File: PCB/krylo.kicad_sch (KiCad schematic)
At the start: 50 parts, among them SW1 Switch, SW10 Switch, SW11 Switch, SW12 Switch, SW13 Switch, SW14 Switch, SW15 Switch, SW16 Switch, SW2 Switch, SW3 Switch, SW4 Switch, SW5 Switch, SW6 Switch, SW7 Switch, SW8 Switch, SW9 Switch, U1 nice_nano

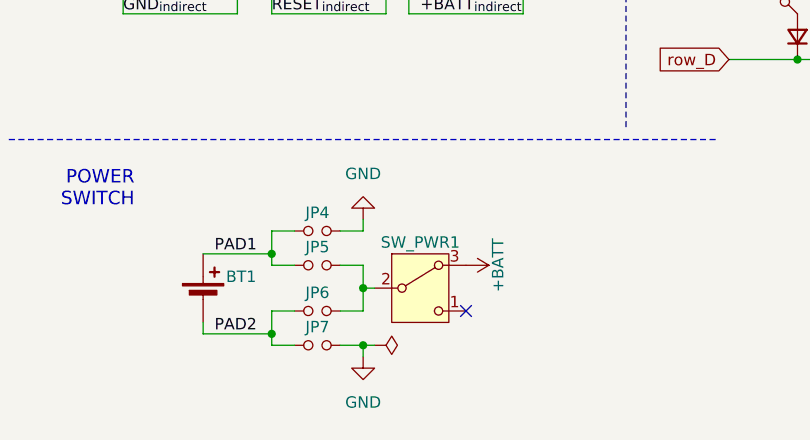
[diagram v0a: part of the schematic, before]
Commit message: Schematic is made so that it contains the double sided PCB configuration. The power component is now (conceptually) contains two switches and routes them accordingly.
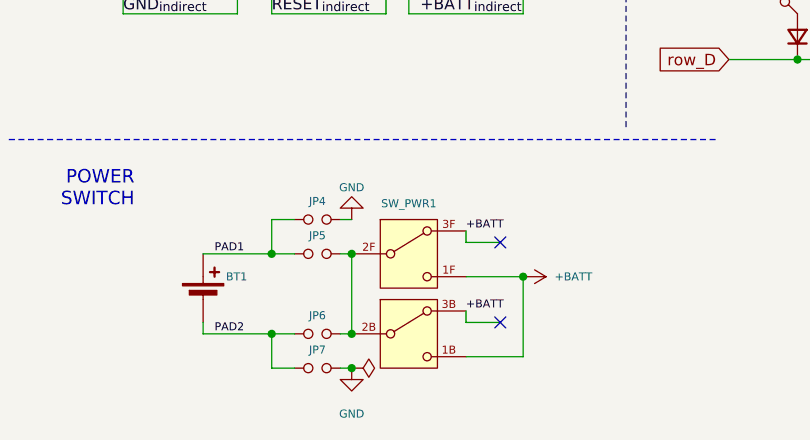
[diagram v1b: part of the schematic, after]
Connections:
- net +BATT: now also SW_PWR1.1B (C_back), SW_PWR1.1F (C_front), SW_PWR1.3B (A_back), SW_PWR1.3F (A_front); no longer SW_PWR1.3 (A)
- net at JP5.2, JP6.2: now also SW_PWR1.2B (B_back), SW_PWR1.2F (B_front); no longer SW_PWR1.2 (B)
- no-connect marks 10 -> 11
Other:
- moved on the sheet: JP4, JP5, JP6, JP7

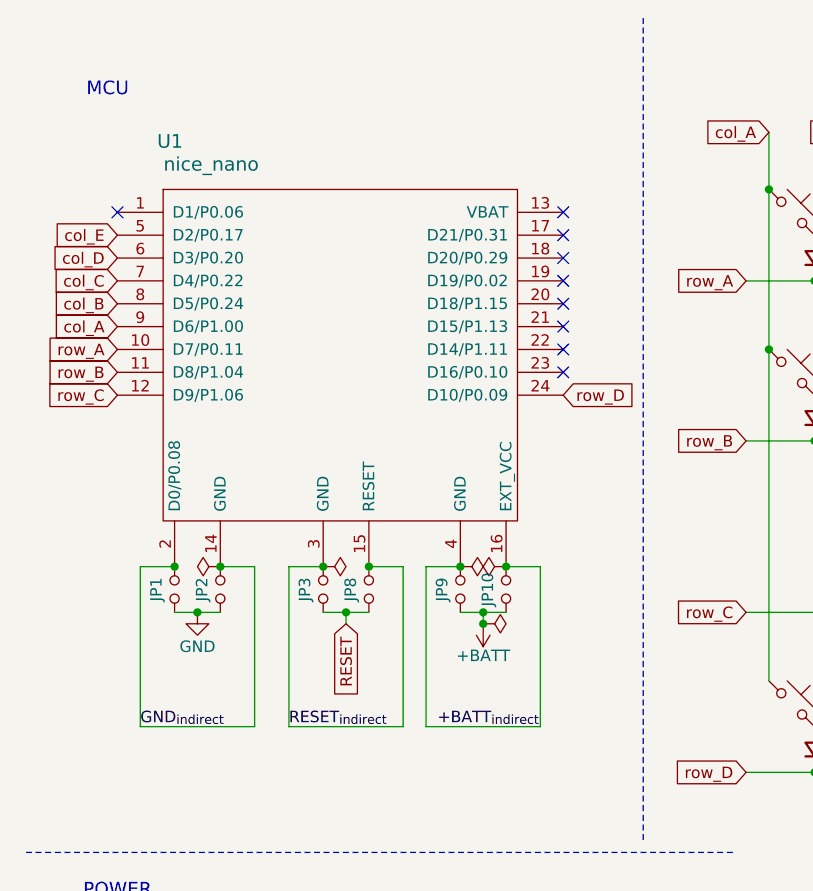
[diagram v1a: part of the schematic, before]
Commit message: Fix: correction of the MCU top/bottom pin usage and placement as well as silkscreen corrections
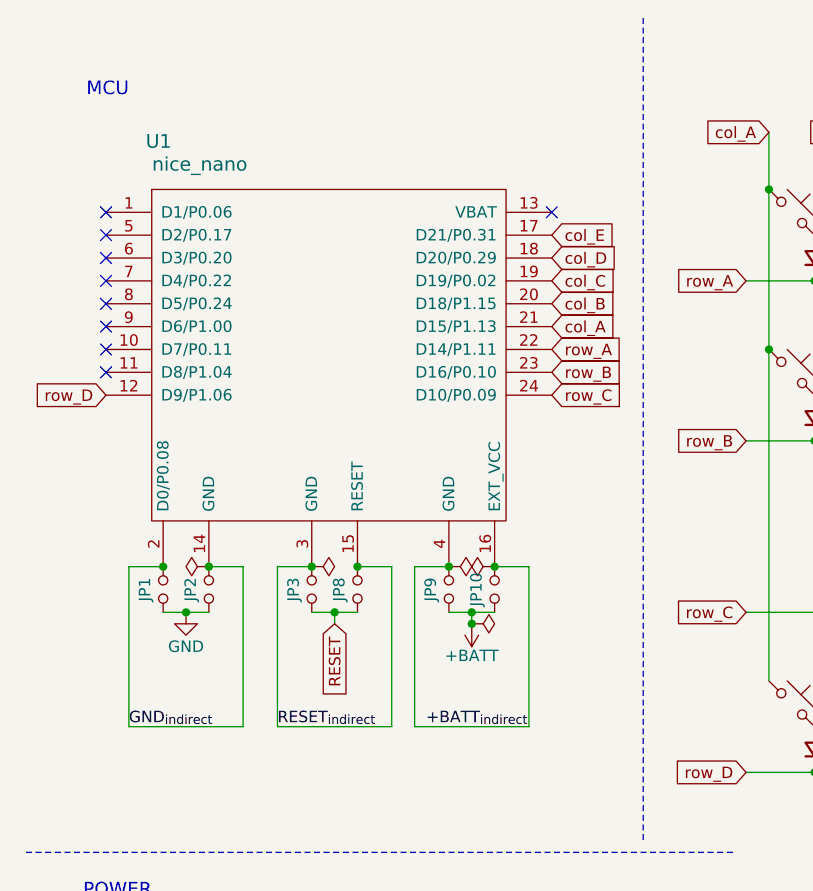
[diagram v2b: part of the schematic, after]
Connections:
- net col_A: now also U1.21 (D15/P1.13); no longer U1.9 (D6/P1.00)
- net col_B: now also U1.20 (D18/P1.15); no longer U1.8 (D5/P0.24)
- net col_C: now also U1.19 (D19/P0.02); no longer U1.7 (D4/P0.22)
- net col_D: now also U1.18 (D20/P0.29); no longer U1.6 (D3/P0.20)
- net col_E: now also U1.17 (D21/P0.31); no longer U1.5 (D2/P0.17)
- net row_A: now also U1.22 (D14/P1.11); no longer U1.10 (D7/P0.11)
- net row_B: now also U1.23 (D16/P0.10); no longer U1.11 (D8/P1.04)
- net row_C: now also U1.24 (D10/P0.09); no longer U1.12 (D9/P1.06)
- net row_D: now also U1.12 (D9/P1.06); no longer U1.24 (D10/P0.09)
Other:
- moved on the sheet: JP1, JP10, JP2, JP3, JP8, JP9, U1

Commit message: Jumper reference numbers are sorted
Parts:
- renumbered JP4 to JP1, JP5 to JP2, JP6 to JP3, JP7 to JP4, JP1 to JP5, JP2 to JP6, JP3 to JP7
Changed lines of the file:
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@@
 		(in_pos_files yes)
 		(dnp no)
-		(property "Reference" "JP1"
+		(property "Reference" "JP5"
 			(at 24.638 74.93 0)
 			(show_name no)
@@
 			(project "krylo"
 				(path "/231ead31-262f-44fe-a25c-f58d2465dcca"
-					(reference "JP1")
+					(reference "JP5")
 					(unit 1)
 				)
@@
 		(in_pos_files yes)
 		(dnp no)
-		(property "Reference" "JP6"
+		(property "Reference" "JP3"
 			(at 45.72 123.698 0)
 			(show_name no)
@@
 			(project "krylo"
 				(path "/231ead31-262f-44fe-a25c-f58d2465dcca"
-					(reference "JP6")
+					(reference "JP3")
 					(unit 1)
 				)
@@
 		(in_pos_files yes)
 		(dnp no)
-		(property "Reference" "JP4"
+		(property "Reference" "JP1"
 			(at 45.72 110.998 0)
 			(show_name no)
@@
 			(project "krylo"
 				(path "/231ead31-262f-44fe-a25c-f58d2465dcca"
-					(reference "JP4")
+					(reference "JP1")
 					(unit 1)
 				)
@@
 		(in_pos_files yes)
 		(dnp no)
-		(property "Reference" "JP2"
+		(property "Reference" "JP6"
 			(at 29.718 74.93 0)
 			(show_name no)
@@
 			(project "krylo"
 				(path "/231ead31-262f-44fe-a25c-f58d2465dcca"
-					(reference "JP2")
+					(reference "JP6")
 					(unit 1)
 				)
@@
 		(in_pos_files yes)
 		(dnp no)
-		(property "Reference" "JP7"
+		(property "Reference" "JP4"
 			(at 45.72 127.508 0)
 			(show_name no)
@@
 			(project "krylo"
 				(path "/231ead31-262f-44fe-a25c-f58d2465dcca"
-					(reference "JP7")
+					(reference "JP4")
 					(unit 1)
 				)
@@
 		(in_pos_files yes)
 		(dnp no)
-		(property "Reference" "JP5"
+		(property "Reference" "JP2"
 			(at 45.72 114.808 0)
 			(show_name no)
@@
 			(project "krylo"
 				(path "/231ead31-262f-44fe-a25c-f58d2465dcca"
-					(reference "JP5")
+					(reference "JP2")
 					(unit 1)
 				)
@@
 		(in_pos_files yes)
 		(dnp no)
-		(property "Reference" "JP3"
+		(property "Reference" "JP7"
 			(at 41.148 74.93 0)
 			(show_name no)
@@
 			(project "krylo"
 				(path "/231ead31-262f-44fe-a25c-f58d2465dcca"
-					(reference "JP3")
+					(reference "JP7")
 					(unit 1)
 				)

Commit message: Jumpers now configure the opposite side. We solder jumpers on the bottom of each side of the split
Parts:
- renumbered JP9 to JP10, JP6 to JP5, JP5 to JP6, JP8 to JP7, JP7 to JP8, JP10 to JP9
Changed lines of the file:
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@@
 		(in_pos_files yes)
 		(dnp no)
-		(property "Reference" "JP5"
+		(property "Reference" "JP6"
 			(at 24.638 74.93 0)
 			(show_name no)
@@
 			(project "krylo"
 				(path "/231ead31-262f-44fe-a25c-f58d2465dcca"
-					(reference "JP5")
+					(reference "JP6")
 					(unit 1)
 				)
@@
 		(in_pos_files yes)
 		(dnp no)
-		(property "Reference" "JP8"
+		(property "Reference" "JP7"
 			(at 46.228 74.93 0)
 			(show_name no)
@@
 			(project "krylo"
 				(path "/231ead31-262f-44fe-a25c-f58d2465dcca"
-					(reference "JP8")
+					(reference "JP7")
 					(unit 1)
 				)
@@
 		(in_pos_files yes)
 		(dnp no)
-		(property "Reference" "JP10"
+		(property "Reference" "JP9"
 			(at 61.468 74.93 0)
 			(show_name no)
@@
 			(project "krylo"
 				(path "/231ead31-262f-44fe-a25c-f58d2465dcca"
-					(reference "JP10")
+					(reference "JP9")
 					(unit 1)
 				)
@@
 		(in_pos_files yes)
 		(dnp no)
-		(property "Reference" "JP9"
+		(property "Reference" "JP10"
 			(at 56.388 74.93 0)
 			(show_name no)
@@
 			(project "krylo"
 				(path "/231ead31-262f-44fe-a25c-f58d2465dcca"
-					(reference "JP9")
+					(reference "JP10")
 					(unit 1)
 				)
@@
 		(in_pos_files yes)
 		(dnp no)
-		(property "Reference" "JP6"
+		(property "Reference" "JP5"
 			(at 29.718 74.93 0)
 			(show_name no)
@@
 			(project "krylo"
 				(path "/231ead31-262f-44fe-a25c-f58d2465dcca"
-					(reference "JP6")
+					(reference "JP5")
 					(unit 1)
 				)
@@
 		(in_pos_files yes)
 		(dnp no)
-		(property "Reference" "JP7"
+		(property "Reference" "JP8"
 			(at 41.148 74.93 0)
 			(show_name no)
@@
 			(project "krylo"
 				(path "/231ead31-262f-44fe-a25c-f58d2465dcca"
-					(reference "JP7")
+					(reference "JP8")
 					(unit 1)
 				)

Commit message: Configuration of the JST connector is also done for on the bottom side of the PCB
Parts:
- renumbered JP4 to JP1, JP3 to JP2, JP2 to JP3, JP1 to JP4
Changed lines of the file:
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@@
 		(in_pos_files yes)
 		(dnp no)
-		(property "Reference" "JP3"
+		(property "Reference" "JP2"
 			(at 45.72 123.698 0)
 			(show_name no)
@@
 			(project "krylo"
 				(path "/231ead31-262f-44fe-a25c-f58d2465dcca"
-					(reference "JP3")
+					(reference "JP2")
 					(unit 1)
 				)
@@
 		(in_pos_files yes)
 		(dnp no)
-		(property "Reference" "JP1"
+		(property "Reference" "JP4"
 			(at 45.72 110.998 0)
 			(show_name no)
@@
 			(project "krylo"
 				(path "/231ead31-262f-44fe-a25c-f58d2465dcca"
-					(reference "JP1")
+					(reference "JP4")
 					(unit 1)
 				)
@@
 		(in_pos_files yes)
 		(dnp no)
-		(property "Reference" "JP4"
+		(property "Reference" "JP1"
 			(at 45.72 127.508 0)
 			(show_name no)
@@
 			(project "krylo"
 				(path "/231ead31-262f-44fe-a25c-f58d2465dcca"
-					(reference "JP4")
+					(reference "JP1")
 					(unit 1)
 				)
@@
 		(in_pos_files yes)
 		(dnp no)
-		(property "Reference" "JP2"
+		(property "Reference" "JP3"
 			(at 45.72 114.808 0)
 			(show_name no)
@@
 			(project "krylo"
 				(path "/231ead31-262f-44fe-a25c-f58d2465dcca"
-					(reference "JP2")
-					(unit 1)
-				)
+					(reference "JP3")
+					(unit 1)
+				)

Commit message: The mounting solution is changed to the solderable M2 nuts. Work in progress
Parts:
- H1, H2, H3, H4: footprint krylo:MountingHole -> krylo:SMT_M2
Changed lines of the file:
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@@
 			)
 		)
-		(property "Footprint" "krylo:MountingHole"
+		(property "Footprint" "krylo:SMT_M2"
 			(at 170.18 40.64 0)
 			(hide yes)
@@
 			)
 		)
-		(property "Footprint" "krylo:MountingHole"
+		(property "Footprint" "krylo:SMT_M2"
 			(at 170.18 34.29 0)
 			(hide yes)
@@
 			)
 		)
-		(property "Footprint" "krylo:MountingHole"
+		(property "Footprint" "krylo:SMT_M2"
 			(at 170.18 27.94 0)
 			(hide yes)
@@
 			)
 		)
-		(property "Footprint" "krylo:MountingHole"
+		(property "Footprint" "krylo:SMT_M2"
 			(at 170.18 47.244 0)
 			(hide yes)

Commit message: Added fifth mount point and edited the edges to contain the updated mounts
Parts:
- added H5: MountingHole, krylo:SMT_M2, symbol krylo:MountingHole
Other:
- moved on the sheet: H1, H2, H3, H4
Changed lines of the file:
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@@
 	(symbol
 		(lib_id "krylo:MountingHole")
-		(at 170.18 40.64 0)
+		(at 170.18 36.576 0)
 		(unit 1)
 		(body_style 1)
@@
 		(fields_autoplaced yes)
 		(property "Reference" "H3"
-			(at 172.72 39.3699 0)
+			(at 172.72 35.3059 0)
 			(show_name no)
 			(do_not_autoplace no)
@@
 		)
 		(property "Value" "MountingHole"
-			(at 172.72 41.9099 0)
+			(at 172.72 37.8459 0)
 			(show_name no)
 			(do_not_autoplace no)
@@
 		)
 		(property "Footprint" "krylo:SMT_M2"
-			(at 170.18 40.64 0)
-			(hide yes)
-			(show_name no)
-			(do_not_autoplace no)
-			(effects
-				(font
-					(size 1.27 1.27)
-				)
-			)
-		)
-		(property "Datasheet" ""
-			(at 170.18 40.64 0)
+			(at 170.18 36.576 0)
+			(hide yes)
+			(show_name no)
+			(do_not_autoplace no)
+			(effects
+				(font
+					(size 1.27 1.27)
+				)
+			)
+		)
+		(property "Datasheet" ""
+			(at 170.18 36.576 0)
 			(hide yes)
 			(show_name no)
@@
 		)
 		(property "Description" "M2 mounting hole"
-			(at 170.18 40.64 0)
+			(at 170.18 36.576 0)
 			(hide yes)
 			(show_name no)
@@
 	(symbol
 		(lib_id "krylo:MountingHole")
-		(at 170.18 34.29 0)
+		(at 170.18 30.226 0)
 		(unit 1)
 		(body_style 1)
@@
 		(fields_autoplaced yes)
 		(property "Reference" "H2"
-			(at 172.72 33.0199 0)
+			(at 172.72 28.9559 0)
 			(show_name no)
 			(do_not_autoplace no)
@@
 		)
 		(property "Value" "MountingHole"
-			(at 172.72 35.5599 0)
+			(at 172.72 31.4959 0)
 			(show_name no)
 			(do_not_autoplace no)
@@
 		)
 		(property "Footprint" "krylo:SMT_M2"
-			(at 170.18 34.29 0)
-			(hide yes)
-			(show_name no)
-			(do_not_autoplace no)
-			(effects
-				(font
-					(size 1.27 1.27)
-				)
-			)
-		)
-		(property "Datasheet" ""
-			(at 170.18 34.29 0)
+			(at 170.18 30.226 0)
+			(hide yes)
+			(show_name no)
+			(do_not_autoplace no)
+			(effects
+				(font
+					(size 1.27 1.27)
+				)
+			)
+		)
+		(property "Datasheet" ""
+			(at 170.18 30.226 0)
 			(hide yes)
 			(show_name no)
@@
 		)
 		(property "Description" "M2 mounting hole"
-			(at 170.18 34.29 0)
+			(at 170.18 30.226 0)
 			(hide yes)
 			(show_name no)
@@
 	(symbol
 		(lib_id "krylo:MountingHole")
-		(at 170.18 27.94 0)
+		(at 170.18 23.876 0)
 		(unit 1)
 		(body_style 1)
@@
 		(fields_autoplaced yes)
 		(property "Reference" "H1"
-			(at 172.72 26.6699 0)
+			(at 172.72 22.6059 0)
 			(show_name no)
 			(do_not_autoplace no)
@@
 		)
 		(property "Value" "MountingHole"
-			(at 172.72 29.2099 0)
+			(at 172.72 25.1459 0)
 			(show_name no)
 			(do_not_autoplace no)
@@
 		)
 		(property "Footprint" "krylo:SMT_M2"
-			(at 170.18 27.94 0)
-			(hide yes)
-			(show_name no)
-			(do_not_autoplace no)
-			(effects
-				(font
-					(size 1.27 1.27)
-				)
-			)
-		)
-		(property "Datasheet" ""
-			(at 170.18 27.94 0)
+			(at 170.18 23.876 0)
+			(hide yes)
+			(show_name no)
+			(do_not_autoplace no)
+			(effects
+				(font
+					(size 1.27 1.27)
+				)
+			)
+		)
+		(property "Datasheet" ""
+			(at 170.18 23.876 0)
 			(hide yes)
 			(show_name no)
@@
 		)
 		(property "Description" "M2 mounting hole"
-			(at 170.18 27.94 0)
+			(at 170.18 23.876 0)
 			(hide yes)
 			(show_name no)
@@
 	)
 	(symbol
+		(lib_id "krylo:MountingHole")
+		(at 170.18 49.53 0)
+		(unit 1)
+		(body_style 1)
+		(exclude_from_sim no)
+		(in_bom no)
+		(on_board yes)
+		(in_pos_files yes)
+		(dnp no)
+		(fields_autoplaced yes)
+		(property "Reference" "H5"
+			(at 172.72 48.2599 0)
+			(show_name no)
+			(do_not_autoplace no)
+			(effects
+				(font
+					(size 1.27 1.27)
+				)
+				(justify left)
+			)
+		)
+		(property "Value" "MountingHole"
+			(at 172.72 50.7999 0)
+			(show_name no)
+			(do_not_autoplace no)
+			(effects
+				(font
+					(size 1.27 1.27)
+				)
+				(justify left)
+			)
+		)
+		(property "Footprint" "krylo:SMT_M2"
+			(at 170.18 49.53 0)
+			(hide yes)
+			(show_name no)
+			(do_not_autoplace no)
+			(effects
+				(font
+					(size 1.27 1.27)
+				)
+			)
+		)
+		(property "Datasheet" ""
+			(at 170.18 49.53 0)
+			(hide yes)
+			(show_name no)
+			(do_not_autoplace no)
+			(effects
+				(font
+					(size 1.27 1.27)
+				)
+			)
+		)
+		(property "Description" "M2 mounting hole"
+			(at 170.18 49.53 0)
+			(hide yes)
+			(show_name no)
+			(do_not_autoplace no)
+			(effects
+				(font
+					(size 1.27 1.27)
+				)
+			)
+		)
+		(instances
+			(project "krylo"
+				(path "/231ead31-262f-44fe-a25c-f58d2465dcca"
+					(reference "H5")
+					(unit 1)
+				)
+			)
+		)
+	)
+	(symbol
 		(lib_id "krylo:Switch")
 		(at 129.54 33.02 0)
@@
 	(symbol
 		(lib_id "krylo:MountingHole")
-		(at 170.18 47.244 0)
+		(at 170.18 43.18 0)
 		(unit 1)
 		(body_style 1)
@@
 		(fields_autoplaced yes)
 		(property "Reference" "H4"
-			(at 172.72 45.9739 0)
+			(at 172.72 41.9099 0)
 			(show_name no)
 			(do_not_autoplace no)
@@
 		)
 		(property "Value" "MountingHole"
-			(at 172.72 48.5139 0)
+			(at 172.72 44.4499 0)
 			(show_name no)
 			(do_not_autoplace no)
@@
 		)
 		(property "Footprint" "krylo:SMT_M2"
-			(at 170.18 47.244 0)
-			(hide yes)
-			(show_name no)
-			(do_not_autoplace no)
-			(effects
-				(font
-					(size 1.27 1.27)
-				)
-			)
-		)
-		(property "Datasheet" ""
-			(at 170.18 47.244 0)
+			(at 170.18 43.18 0)
+			(hide yes)
+			(show_name no)
+			(do_not_autoplace no)
+			(effects
+				(font
+					(size 1.27 1.27)
+				)
+			)
+		)
+		(property "Datasheet" ""
+			(at 170.18 43.18 0)
 			(hide yes)
 			(show_name no)
@@
 		)
 		(property "Description" "M2 mounting hole"
-			(at 170.18 47.244 0)
-			(hide yes)
-			(show_name no)
+			(at 170.18 43.18 0)
+			(hide yes)
+			(show_name no)

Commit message: Added a molex connector in place of the jst one
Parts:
- BT1: footprint krylo:JST_PH -> krylo:Molex_connector
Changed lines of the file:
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@@
 			)
 		)
-		(property "Footprint" "krylo:JST_PH"
+		(property "Footprint" "krylo:Molex_connector"
 			(at 33.02 120.396 90)
 			(hide yes)
